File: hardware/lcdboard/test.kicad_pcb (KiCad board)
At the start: 2 copper layers, 45.6 x 91.2 mm, 23 parts, among them J1 Conn_01x11_Female, J2 Conn_01x08_Shielded, J3 Conn_01x45, J4 Conn_01x11_Female, U1 AP2502

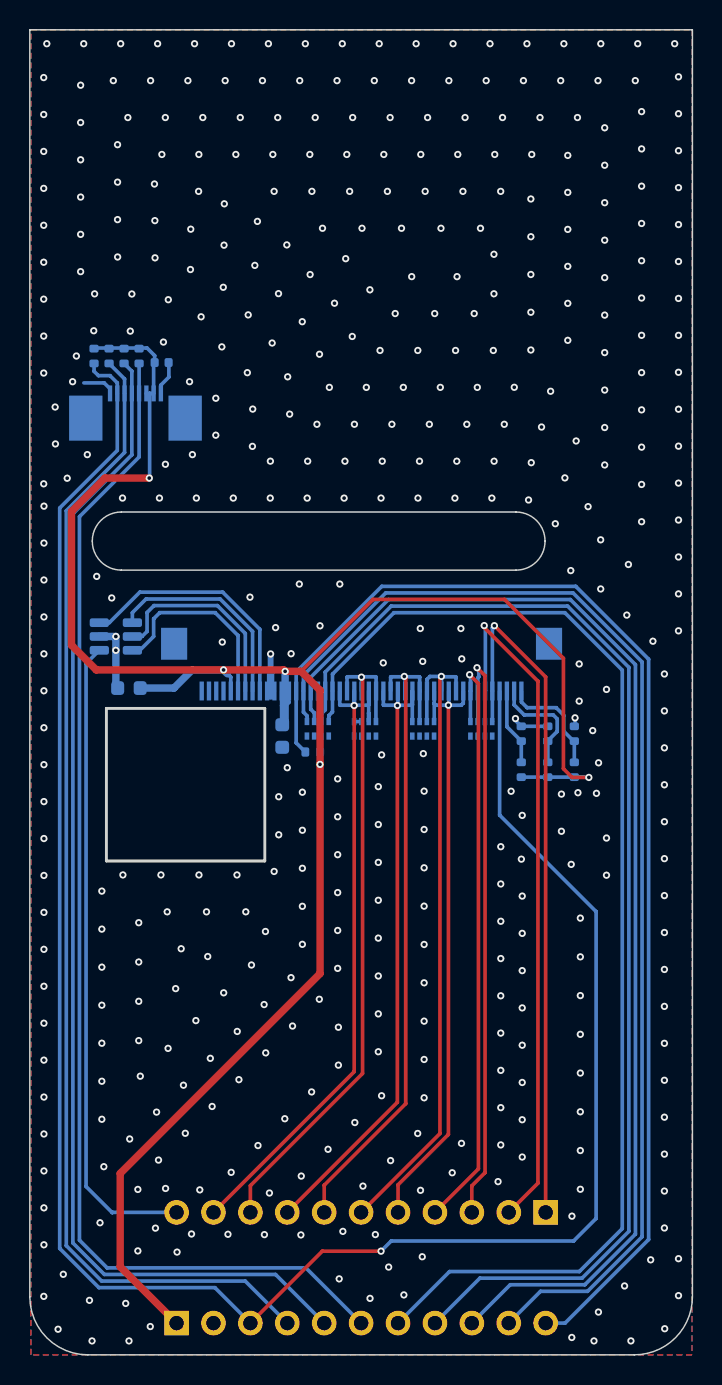
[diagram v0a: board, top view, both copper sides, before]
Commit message: restructure, adding branch for mux'd display board
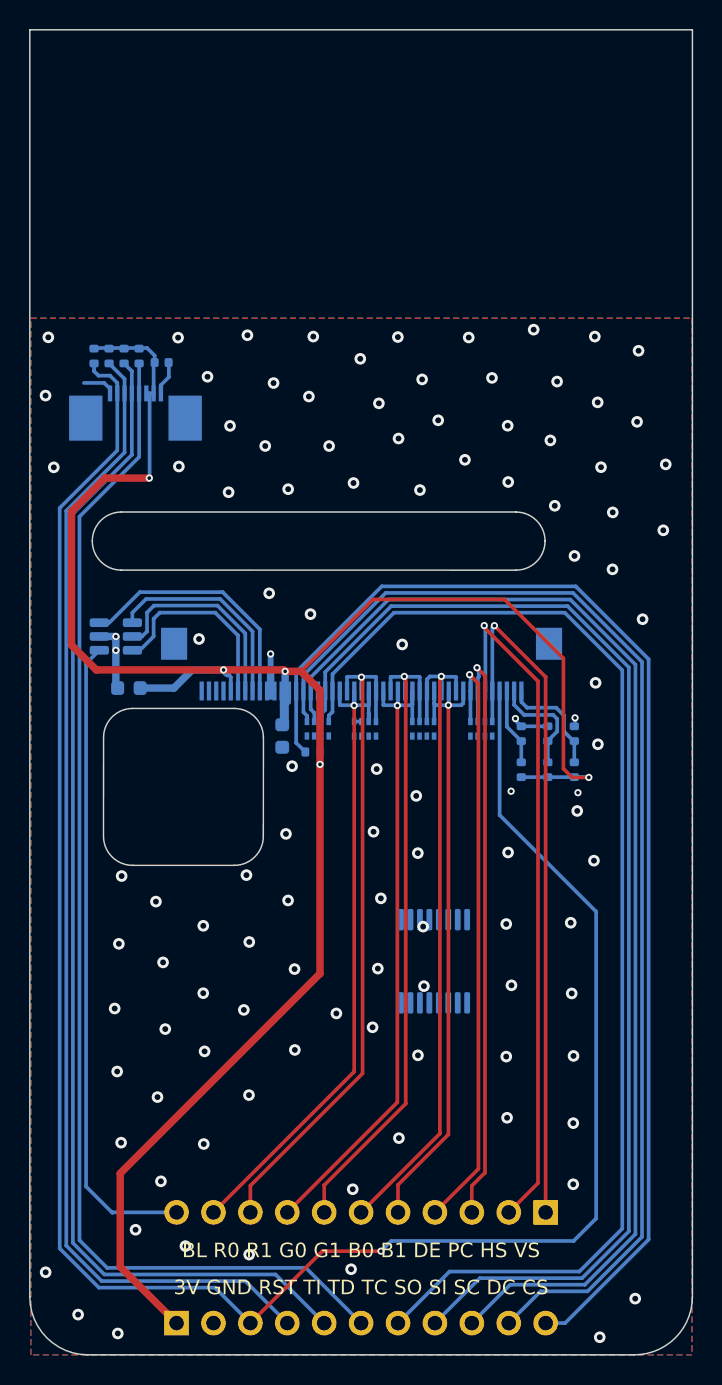
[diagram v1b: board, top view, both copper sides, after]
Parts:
- added U2: 74LS157, Package_SO:TSSOP-16_4.4x5mm_P0.65mm, B.Cu at (70.8, 102.6)
- renumbered C2 to C1, C3 to C2, C4 to C3, J3 to J1, J4 to J3, J1 to J4, R11 to R1, R3 to R10, R7 to R11, R1 to R2, R2 to R3, R9 to R4, R4 to R5, R8 to R7, R10 to R8, R5 to R9, RN3 to RN1, RN4 to RN3, RN1 to RN4
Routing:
- net GND: vias 465 -> 113
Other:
- outline, holes or cut-outs redrawn
- board text added: "3V GND RST TI TD TC SO SI SC DC CS"
- board text added: "BL R0 R1 G0 G1 B0 B1 DE PC HS VS"

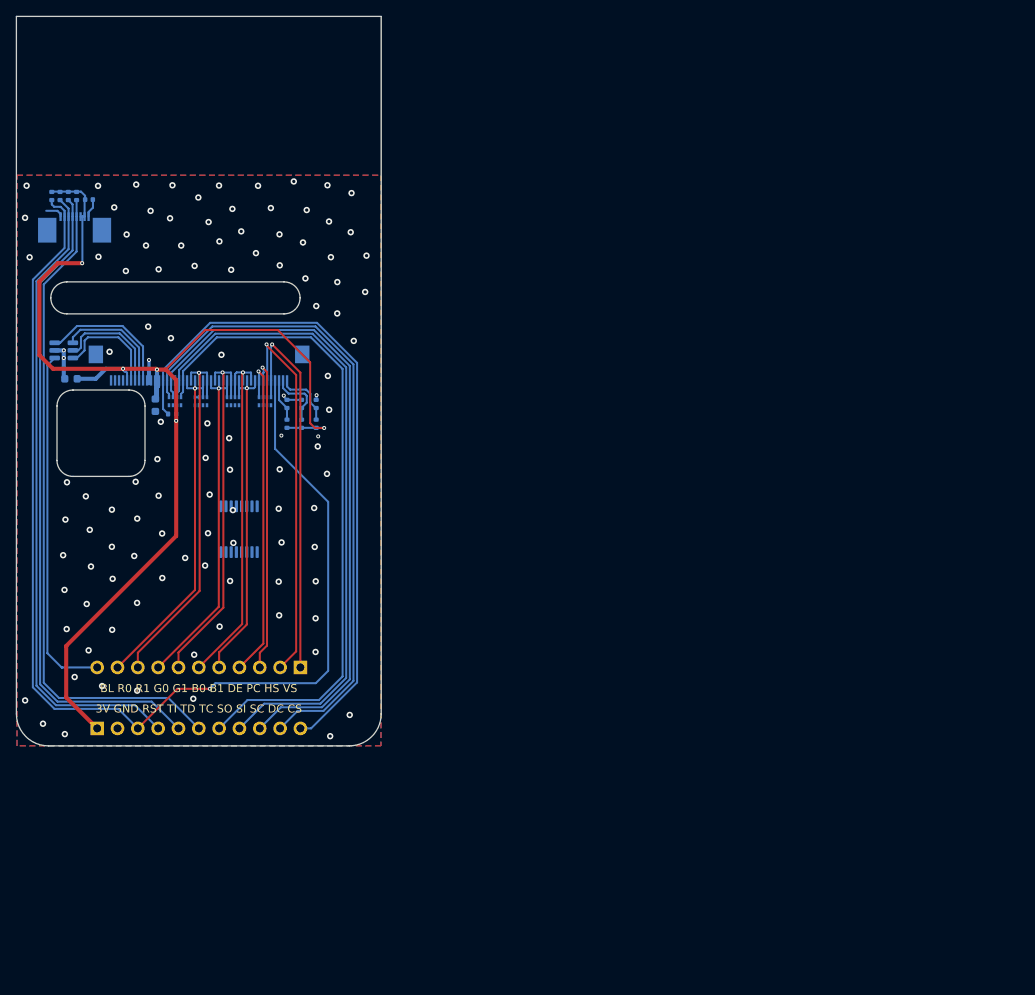
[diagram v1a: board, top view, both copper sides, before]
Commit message: split back out condensed board into lcdboard and base
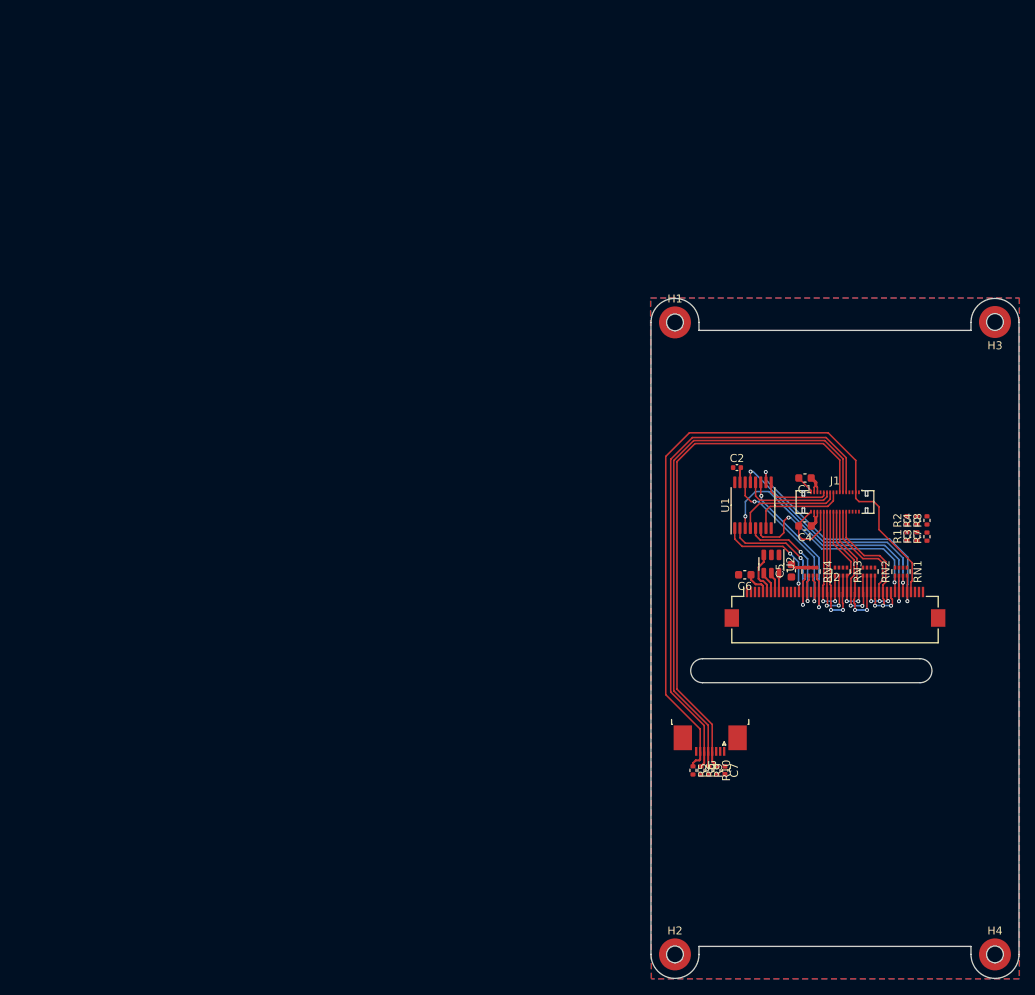
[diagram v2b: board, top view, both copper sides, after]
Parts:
- removed C3: 1u, Capacitor_SMD:C_0603_1608Metric
- removed J4: Conn_01x11_Female, Connector_PinHeader_2.54mm:PinHeader_1x11_P2.54mm_Vertical
- removed R11: 100k, Resistor_SMD:R_0402_1005Metric
- added C4: 1u, Capacitor_SMD:C_0603_1608Metric, F.Cu at (141.5, 102.2)
- added C5: 1u, Capacitor_SMD:C_0603_1608Metric, F.Cu at (139.8, 107.8)
- added C6: 1u, Capacitor_SMD:C_0603_1608Metric, F.Cu at (134.0, 108.3)
- added C7: 0.1u, Capacitor_SMD:C_0402_1005Metric, F.Cu at (131.5, 132.7)
- added H1: TL, Mounting_Wuerth:Mounting_Wuerth_WA-SMSI-M1.6_H2mm_9774020633, F.Cu at (125.2, 76.8)
- added H2: BL, Mounting_Wuerth:Mounting_Wuerth_WA-SMSI-M1.6_H2mm_9774020633, F.Cu at (125.2, 155.8)
- added H3: TR, Mounting_Wuerth:Mounting_Wuerth_WA-SMSI-M1.6_H2mm_9774020633, F.Cu at (165.2, 76.7)
- added H4: BR, Mounting_Wuerth:Mounting_Wuerth_WA-SMSI-M1.6_H2mm_9774020633, F.Cu at (165.3, 155.7)
- C1: value 0.1u -> 1u; footprint Capacitor_SMD:C_0402_1005Metric -> Capacitor_SMD:C_0603_1608Metric; moved to F.Cu
- C2: value 1u -> 0.1u; footprint Capacitor_SMD:C_0603_1608Metric -> Capacitor_SMD:C_0402_1005Metric; moved to F.Cu
- J1: value Conn_01x45 -> Conn_02x16_Odd_Even_MountingPin; footprint Connector_FFC-FPC:Hirose_FH12-45S-0.5SH_1x45-1MP_P0.50mm_Horizontal -> Connector_Molex:Molex_SlimStack_502426-3210_2x16_P0.40mm_Vertical; moved to F.Cu
- J2: value Conn_01x08_Shielded -> Conn_01x45_Shielded; footprint Connector_FFC-FPC:TE_0-1734839-8_1x08-1MP_P0.5mm_Horizontal -> Connector_FFC-FPC:Hirose_FH12-45S-0.5SH_1x45-1MP_P0.50mm_Horizontal; moved to F.Cu
- J3: value Conn_01x11_Female -> CapTouch; footprint Connector_PinHeader_2.54mm:PinHeader_1x11_P2.54mm_Vertical -> Connector_FFC-FPC:TE_0-1734839-8_1x08-1MP_P0.5mm_Horizontal; moved to F.Cu
- R1, R2, R3, R4, R8: value 4.7k -> 100k; moved to F.Cu
- R10, R5, R6, R9: value 100k -> 4.7k; moved to F.Cu
- R7, RN1, RN2, RN3, RN4: moved to F.Cu
- U1: value AP2502 -> 74CBTLV3257; footprint Package_TO_SOT_SMD:SOT-23-6 -> Package_SO:TSSOP-16_4.4x5mm_P0.65mm; moved to F.Cu
- U2: value 74LS157 -> AP2502; footprint Package_SO:TSSOP-16_4.4x5mm_P0.65mm -> Package_TO_SOT_SMD:SOT-23-6; moved to F.Cu
- moved R4 115.5 mm to (155.5, 101.5)
- moved R3 114.3 mm to (155.5, 103.5)
- moved R1 114.1 mm to (154.2, 103.5)
- moved R2 111.4 mm to (154.2, 101.5)
- moved J2 106.2 mm to (145.2, 112.3), turned to 0 degrees
- moved C1 96.0 mm to (141.5, 96.2), turned to 180 degrees
- moved R8 95.3 mm to (156.8, 101.5), turned to 90 degrees
- moved U1 88.3 mm to (135.0, 99.6), turned to 90 degrees
- moved RN1 86.2 mm to (153.5, 107.9)
- moved RN3 82.8 mm to (146.0, 107.9)
- moved RN4 82.3 mm to (142.2, 107.9)
- moved J1 81.3 mm to (145.2, 99.2)
- moved RN2 78.4 mm to (149.5, 107.9)
- moved R7 78.1 mm to (156.8, 103.5)
- moved C2 73.1 mm to (133.0, 94.9), turned to 0 degrees
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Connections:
- C1 pad 1: +3V3 -> VDD_AUX_3V3
- C2 pad 1: +3V3 -> VDD_AUX_3V3
- J1 pad 1: /IM0 -> GND
- J1 pad 10: /B0 -> /LCD_RGB.B1
- J1 pad 11: /B1 -> /TOUCH_SDA
- J1 pad 12: /B0 -> /LCD_RGB.B0
- J1 pad 13: /B1 -> /TOUCH_SCL
- J1 pad 14: /B0 -> /LCD_RGB.G2
- J1 pad 15: /G1 -> /LCD_SPI_CS
- J1 pad 16: /G0 -> /LCD_RGB.G1
- J1 pad 17: /G1 -> /LCD_MUX0
- J1 pad 18: /G0 -> /LCD_RGB.G0
- J1 pad 19: /G1 -> /LCD_MUX1
- J1 pad 2: /IM1 -> GND
- J1 pad 20: /G0 -> /LCD_RGB.R2
- J1 pad 21: /R1 -> /LCD_MUX2
- J1 pad 22: /R0 -> /LCD_RGB.R1
- J1 pad 23: /R1 -> /LCD_MUX3
- J1 pad 24: /R0 -> /LCD_RGB.R0
- J1 pad 25: /R1 -> GND
- J1 pad 26: /R0 -> GND
- J1 pad 27: /MISO -> VDD_AUX_3V3
- J1 pad 28: /MOSI -> VDD_NVDC
- J1 pad 29: /RD -> VDD_AUX_3V3
- J1 pad 3: /IM2 -> ~{RESET}
- J1 pad 30: /SCLK -> VDD_NVDC
- J1 pad 31: /RS -> GND
- J1 pad 32: /CS -> GND
- J1 pad 4: /RESET -> unconnected-(J1-Pad4)
- J1 pad 5: /VSYNC -> /DISPLAY_BL
- J1 pad 6: /HSYNC -> unconnected-(J1-Pad6)
- J1 pad 7: /PCLK -> GND
- J1 pad 8: /DE -> GND
- J1 pad 9: /B1 -> /TOUCH_INT
- J2 pad 1: GND -> unconnected-(J2-Pad1)
- J2 pad 2: +3V3 -> unconnected-(J2-Pad2)
- J2 pad 3: +3V3 -> unconnected-(J2-Pad3)
- J2 pad 4: /TSC_SCL -> unconnected-(J2-Pad4)
- J2 pad 5: /TSC_SDA -> VDD_NVDC
- J2 pad 6: /TSC_INT -> /LCDK4
- J2 pad 7: /RESET -> /LCDK3
- J2 pad 8: GND -> /LCDK2
- J2 pad MP: (no net) -> GND
- J3 pad 1: /VSYNC -> GND
- J3 pad 2: /HSYNC -> VDD_AUX_3V3
- J3 pad 3: /PCLK -> VDD_AUX_3V3
- J3 pad 4: /DE -> /TOUCH_SCL
- J3 pad 5: /B1 -> /TOUCH_SDA
- J3 pad 6: /B0 -> /TOUCH_INT
- J3 pad 7: /G1 -> ~{RESET}
- J3 pad 8: /G0 -> GND
- R1 pad 1: /TSC_INT -> VDD_AUX_3V3
- R1 pad 2: +3V3 -> /IM2
- R10 pad 1: +3V3 -> /TOUCH_SCL
- R10 pad 2: /IM2 -> VDD_AUX_3V3
- R2 pad 1: /TSC_SCL -> /IM2
- R2 pad 2: +3V3 -> GND
- R3 pad 1: /TSC_SDA -> VDD_AUX_3V3
- R3 pad 2: +3V3 -> /IM1
- R4 pad 1: /RESET -> /IM1
- R4 pad 2: +3V3 -> GND
- R5 pad 1: /IM2 -> ~{RESET}
- R5 pad 2: GND -> VDD_AUX_3V3
- R6 pad 1: /IM1 -> /TOUCH_INT
- R6 pad 2: GND -> VDD_AUX_3V3
- R7 pad 1: /IM0 -> VDD_AUX_3V3
- R7 pad 2: GND -> /IM0
- R8 pad 1: /CS -> /IM0
- R8 pad 2: +3V3 -> GND
- R9 pad 1: +3V3 -> /TOUCH_SDA
- R9 pad 2: /IM1 -> VDD_AUX_3V3
- RN1 pad 1: /G0 -> GND
- RN1 pad 2: /G1 -> GND
- RN1 pad 3: /B0 -> GND
- RN1 pad 4: /B1 -> GND
- RN1 pad 5: GND -> /LCD_CTRL.DE
- RN1 pad 6: GND -> /LCD_CTRL.PCLK
- RN1 pad 7: GND -> /LCD_CTRL.HSYNC
- RN1 pad 8: GND -> /LCD_CTRL.VSYNC
- RN2 pad 1: /DE -> GND
- RN2 pad 2: /PCLK -> GND
- RN2 pad 3: /HSYNC -> GND
- RN2 pad 4: /VSYNC -> GND
- RN2 pad 5: GND -> /LCD_RGB.G1
- RN2 pad 6: GND -> /LCD_RGB.G2
- RN2 pad 7: GND -> /LCD_RGB.B0
- RN2 pad 8: GND -> /LCD_RGB.B1
- RN3 pad 3: /R0 -> GND
- RN3 pad 4: /R1 -> GND
- RN3 pad 5: GND -> /LCD_RGB.R0
- RN3 pad 6: GND -> /LCD_RGB.R1
- RN3 pad 7: GND -> /LCD_RGB.R2
- RN3 pad 8: GND -> /LCD_RGB.G0
- RN4 pad 1: /RS -> GND
- RN4 pad 2: /SCLK -> GND
- RN4 pad 3: /MOSI -> GND
- RN4 pad 4: /MISO -> GND
- RN4 pad 5: GND -> /LCD_SPI.DC
- RN4 pad 6: GND -> /LCD_SPI.SCLK
- RN4 pad 7: GND -> /LCD_SPI.MOSI
- RN4 pad 8: GND -> /LCD_SPI.MISO
- U1 pad 1: /BL_PWM -> /LCD_SPI_CS
- U1 pad 2: GND -> /LCD_SPI.DC
- U1 pad 3: /LCDK4 -> /LCD_CTRL.PCLK
- U1 pad 4: /LCDK3 -> /LCD_MUX1
- U1 pad 5: /LCDK2 -> /LCD_SPI.SCLK
- U1 pad 6: /LCDK1 -> /LCD_CTRL.DE
- U2 pad 1: unconnected-(U2-Pad1) -> /DISPLAY_BL
- U2 pad 2: unconnected-(U2-Pad2) -> GND
- U2 pad 3: unconnected-(U2-Pad3) -> /LCDK4
- U2 pad 4: unconnected-(U2-Pad4) -> /LCDK3
- U2 pad 5: unconnected-(U2-Pad5) -> /LCDK2
- U2 pad 6: unconnected-(U2-Pad6) -> /LCDK1
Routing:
- net +3V3: track 150.8 -> 0.00 mm, vias 5 -> 0
- net /RESET: track 144.7 -> 0.00 mm, vias 1 -> 0
- net ~{RESET}: track 0.00 -> 88.1 mm
- net /CS: track 83.9 -> 0.00 mm
- net /TSC_SCL: track 83.8 -> 0.00 mm
- net /MISO: track 83.3 -> 0.00 mm
- net /MOSI: track 82.8 -> 0.00 mm
- net /SCLK: track 82.6 -> 0.00 mm
- net /RS: track 82.1 -> 0.00 mm
- net /TSC_SDA: track 82.0 -> 0.00 mm
- net /TSC_INT: track 80.2 -> 0.00 mm
- net /TOUCH_INT: track 0.00 -> 68.7 mm
- net /TOUCH_SDA: track 0.00 -> 67.4 mm
- net /TOUCH_SCL: track 0.00 -> 66.3 mm
- net /HSYNC: track 49.4 -> 0.00 mm, vias 1 -> 0
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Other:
- board size 45.6 x 91.2 mm -> 46 x 85 mm
- board text removed: "3V GND RST TI TD TC SO SI SC DC CS"
- board text removed: "BL R0 R1 G0 G1 B0 B1 DE PC HS VS"
